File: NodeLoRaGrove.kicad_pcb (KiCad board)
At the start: 2 copper layers, 40 x 50 mm, 44 parts, among them P1 PICKIT PROGRAMMER, P2 ICSP, P3 USB, P4 - Battery +, P5 A0, P6 D9, P7 I2C, P8 A2, SW1 RESET, U1 AP2112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

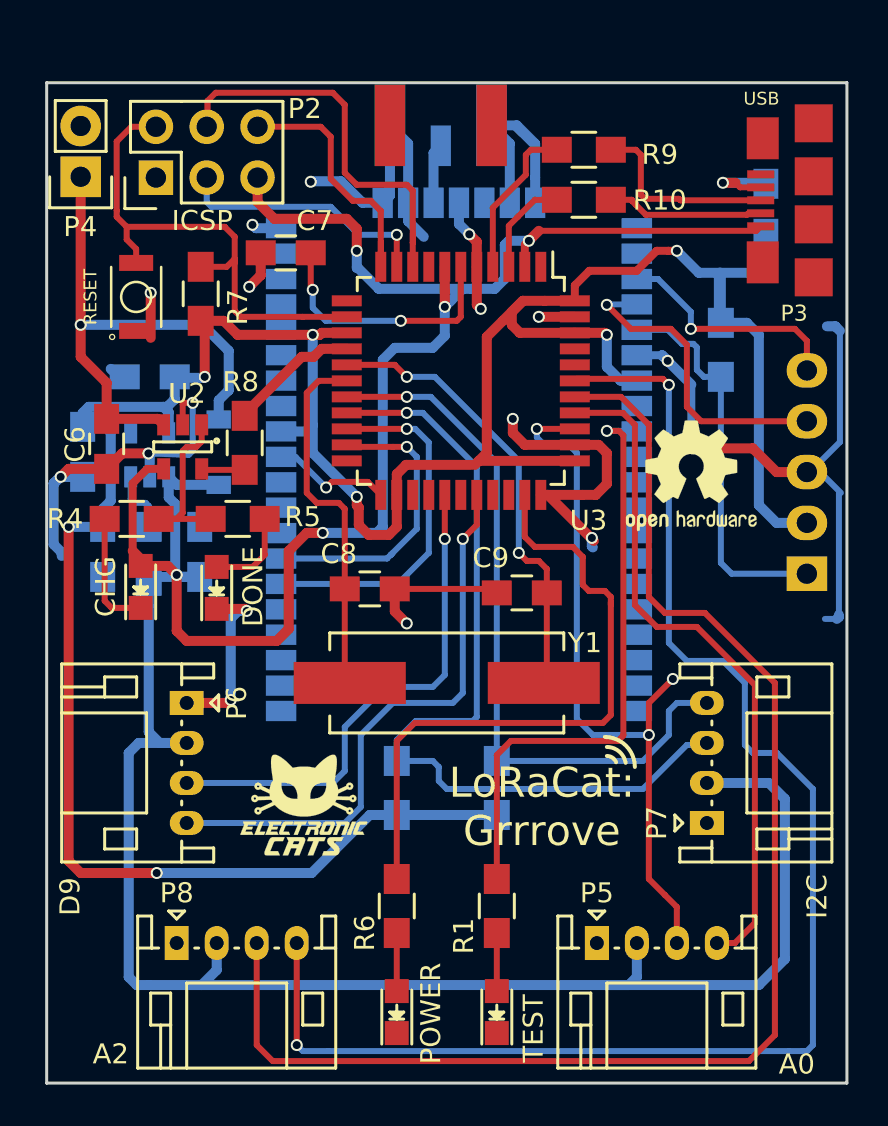
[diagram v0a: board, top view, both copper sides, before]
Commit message: Changed USB
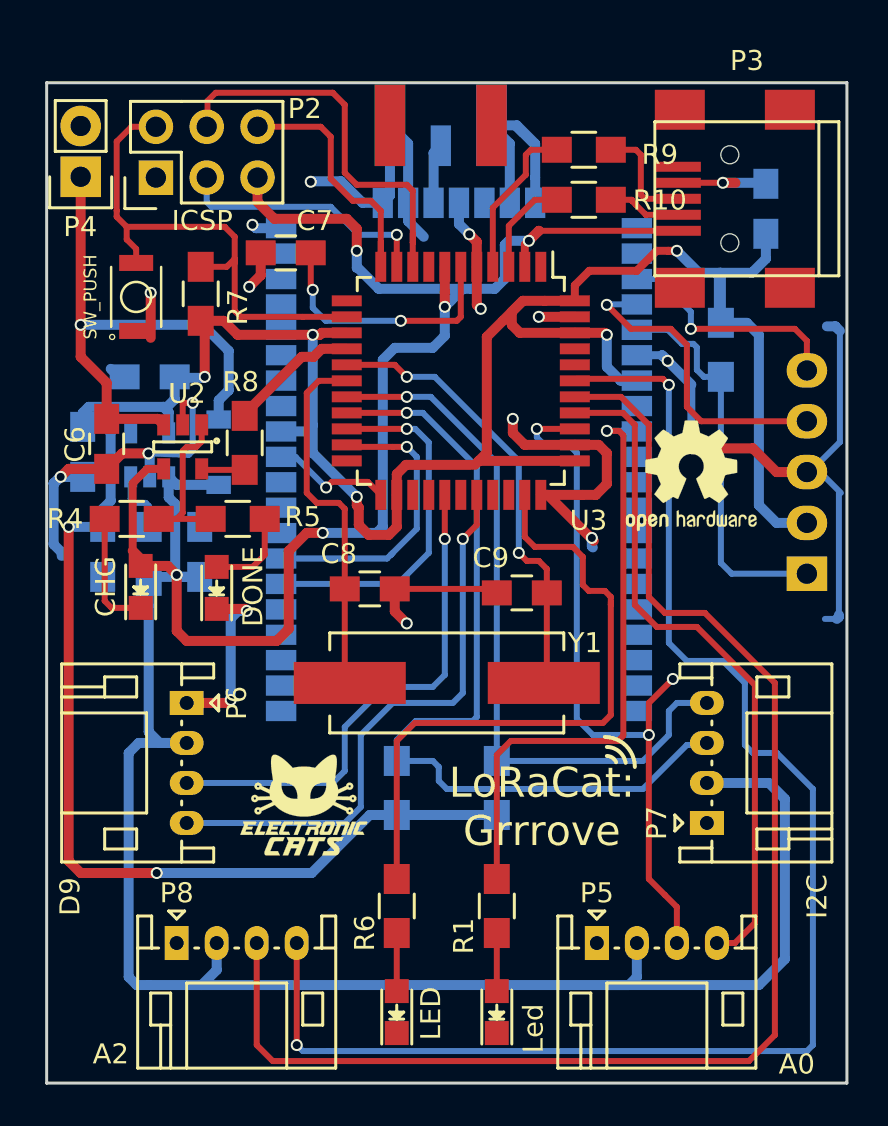
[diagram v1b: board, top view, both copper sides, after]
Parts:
- D2: value TEST -> Led
- D5: value POWER -> LED
- P3: value USB -> USB_A; footprint TIH:10118192-0001LF -> Connect:USB_Mini-B
- P4: value - Battery + -> Battery
- SW1: value RESET -> SW_PUSH
- moved P3 4.79 mm to (159.8, 80.9), turned to 180 degrees
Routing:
- net GND: track 143.3 -> 166.9 mm, vias 19 -> 20
- net Net-(MODULE1-Pad36): track 30.4 -> 7.71 mm, vias 1 -> 0
- net VCC: track 163.8 -> 159.5 mm
- net /D-: track 7.91 -> 3.74 mm
- net /D+: track 9.71 -> 5.69 mm

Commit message: Fix Skilcreen
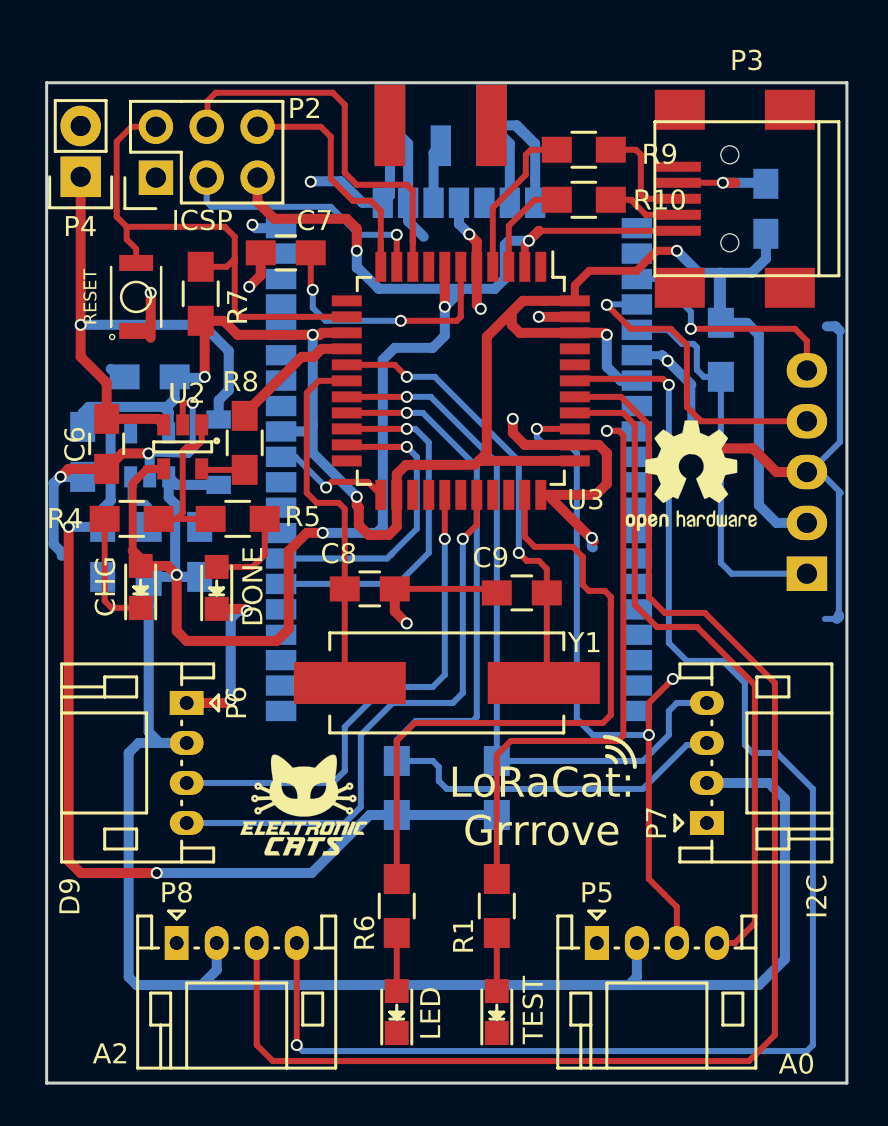
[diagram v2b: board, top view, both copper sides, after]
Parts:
- D2: value Led -> TEST
- SW1: value SW_PUSH -> RESET
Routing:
- net Net-(MODULE1-Pad36): track 7.71 -> 30.4 mm, vias 0 -> 1
- net GND: track 166.9 -> 144.2 mm, vias 20 -> 19
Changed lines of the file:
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@@
 (kicad_pcb (version 4) (host pcbnew 4.0.5)
   (general
-    (links 160)
-    (no_connects 40)
+    (links 120)
+    (no_connects 0)
     (area 124.724999 75.074999 164.875001 125.225001)
     (thickness 1.6)
@@
   )
   (layers
-    (0 F.Cu signal)
-    (31 B.Cu signal)
+    (0 F.Cu signal hide)
+    (31 B.Cu signal hide)
     (32 B.Adhes user)
     (33 F.Adhes user)
@@
       (effects (font (size 1 1) (thickness 0.15)))
     )
-    (fp_text value Led (at -0.81902 1.83 90) (layer F.SilkS)
+    (fp_text value TEST (at 0.10098 1.83 90) (layer F.SilkS)
       (effects (font (size 1 1) (thickness 0.15)))
     )
@@
     (tags "QFP 0.8")
     (attr smd)
-    (fp_text reference U3 (at 6.982 -6.38 360) (layer F.SilkS)
+    (fp_text reference U3 (at 5.95 -6.25 360) (layer F.SilkS)
       (effects (font (size 1 1) (thickness 0.15)))
     )
@@
       (effects (font (size 0.64 0.64) (thickness 0.05)))
     )
-    (fp_text value SW_PUSH (at 0 -2.286 90) (layer F.SilkS)
+    (fp_text value RESET (at 0 -2.286 90) (layer F.SilkS)
       (effects (font (size 0.64 0.64) (thickness 0.1)))
     )
@@
   (segment (start 142.2 100.45) (end 147.1 100.45) (width 0.3) (layer F.Cu) (net 2))
   (segment (start 147.1 100.45) (end 147.3 100.65) (width 0.3) (layer F.Cu) (net 2))
-  (segment (start 153.4 108.05) (end 153.4 107.99999) (width 0.3) (layer F.Cu) (net 2))
-  (segment (start 148 108.05) (end 153.4 108.05) (width 0.3) (layer F.Cu) (net 2))
-  (segment (start 153.4 107.99999) (end 153.625 107.77499) (width 0.3) (layer F.Cu) (net 2))
-  (segment (start 153.625 107.77499) (end 153.625 92.77501) (width 0.3) (layer F.Cu) (net 2))
-  (segment (start 153.625 92.77501) (end 153.39999 92.55) (width 0.3) (layer F.Cu) (net 2))
-  (segment (start 153.39999 92.55) (end 152.8 92.55) (width 0.3) (layer F.Cu) (net 2))
-  (via (at 152.8 92.55) (size 0.6) (drill 0.4) (layers F.Cu B.Cu) (net 2))
-  (segment (start 147.3 108.75) (end 148 108.05) (width 0.3) (layer F.Cu) (net 2))
   (segment (start 156.35 82.5501) (end 149.3999 82.5501) (width 0.3) (layer F.Cu) (net 3))
   (segment (start 149.3999 82.5501) (end 149.39944 82.55056) (width 0.5) (layer F.Cu) (net 3))
@@
   (segment (start 137.3 118.15) (end 137.3 123.25) (width 0.3) (layer F.Cu) (net 30))
   (via (at 137.3 123.25) (size 0.6) (drill 0.4) (layers F.Cu B.Cu) (net 30))
+  (segment (start 153.4 108.05) (end 153.4 107.99999) (width 0.3) (layer F.Cu) (net 31))
+  (segment (start 148 108.05) (end 153.4 108.05) (width 0.3) (layer F.Cu) (net 31))
+  (segment (start 153.4 107.99999) (end 153.625 107.77499) (width 0.3) (layer F.Cu) (net 31))
+  (segment (start 153.625 107.77499) (end 153.625 92.77501) (width 0.3) (layer F.Cu) (net 31))
+  (segment (start 153.625 92.77501) (end 153.39999 92.55) (width 0.3) (layer F.Cu) (net 31))
+  (segment (start 153.39999 92.55) (end 152.8 92.55) (width 0.3) (layer F.Cu) (net 31))
+  (via (at 152.8 92.55) (size 0.6) (drill 0.4) (layers F.Cu B.Cu) (net 31))
+  (segment (start 147.3 108.75) (end 148 108.05) (width 0.3) (layer F.Cu) (net 31))
   (segment (start 147.3 114.95) (end 147.3 108.75) (width 0.3) (layer F.Cu) (net 31))
   (segment (start 152.8 92.55) (end 154.268262 92.55) (width 0.3) (layer B.Cu) (net 31))
